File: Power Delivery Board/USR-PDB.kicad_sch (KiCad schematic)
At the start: 32 parts, among them U1 XT90, U10 Anderson PP45 Vert. 2x1, U11 Anderson PP45 Vert. 2x1, U12 TL2575HV-05IKV, U13 MCP3002-I/P, U2 LM2676T-12_NOPB, U5 Anderson PP45 Vert. 2x1, U6 Anderson PP45 Vert. 2x1, U7 Anderson PP45 Vert. 2x1, U8 Anderson PP45 Vert. 2x1, U9 Anderson PP45 Vert. 2x1

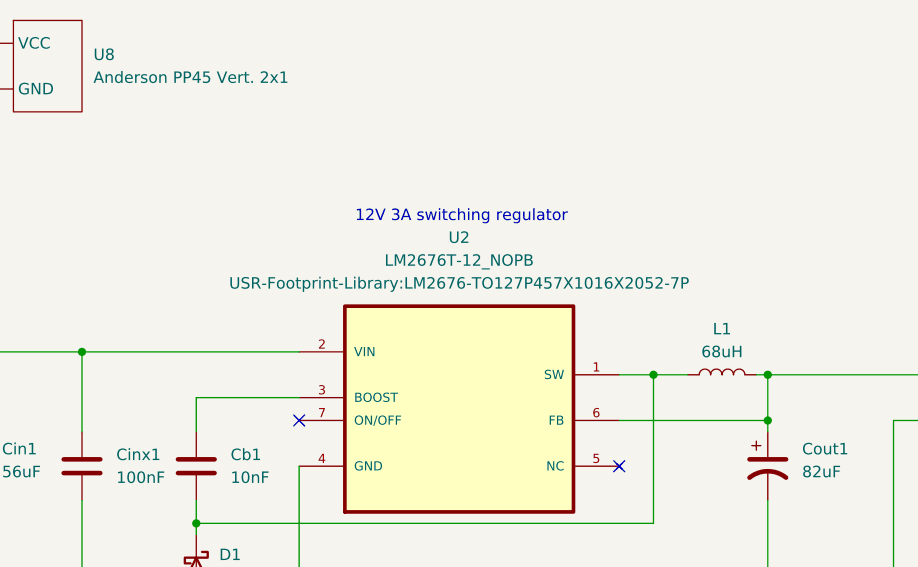
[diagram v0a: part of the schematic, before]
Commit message: Added datasheets and associated footprints to symbols
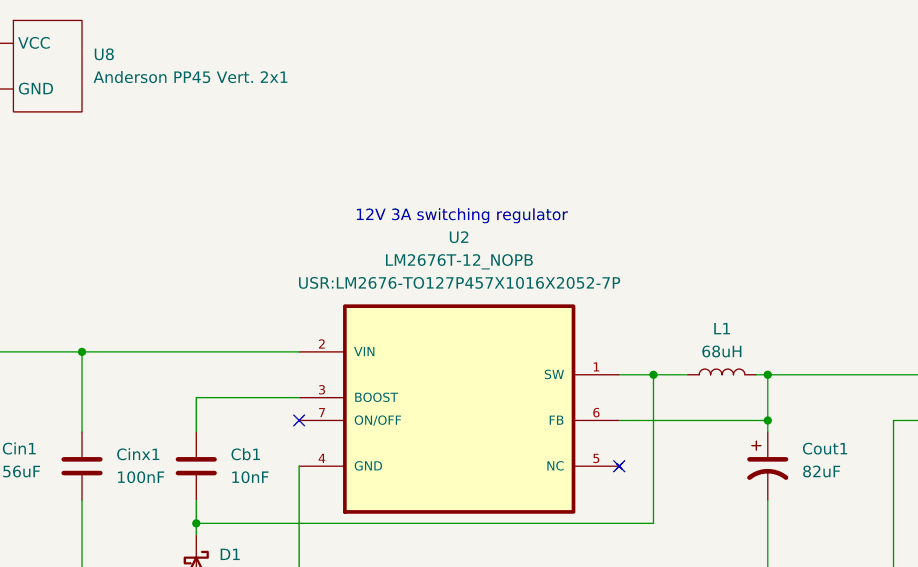
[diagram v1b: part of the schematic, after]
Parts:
- F1, F2, F3, F4, F5, F6, F7: footprint USR-Footprint-Library:FUSE_3557-15 -> USR:FUSE_3557-15
- U10, U11, U5, U6, U7, U8, U9: footprint USR-Footprint-Library:ANDERSON PP45 VERT. 2X1 -> USR:ANDERSON PP45 VERT. 2X1
- U12: footprint USR-Footprint-Library:TL2575HV-05IKV -> USR:TL2575HV-05IKV
- U13: footprint USR-Footprint-Library:PDIP8_300MC_MCH -> USR:PDIP8_300MC_MCH
- U2: footprint USR-Footprint-Library:LM2676-TO127P457X1016X2052-7P -> USR:LM2676-TO127P457X1016X2052-7P
- U3, U4: footprint USR-Footprint-Library:LKSR 50-NP -> USR:LKSR 50-NP
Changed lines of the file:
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@@
 			)
 		)
-		(property "Footprint" "USR-Footprint-Library:ANDERSON PP45 VERT. 2X1"
+		(property "Footprint" "USR:ANDERSON PP45 VERT. 2X1"
 			(at 187.96 81.28 0)
 			(effects
@@
 			)
 		)
-		(property "Footprint" "USR-Footprint-Library:FUSE_3557-15"
+		(property "Footprint" "USR:FUSE_3557-15"
 			(at 49.53 138.43 0)
 			(effects
@@
 			)
 		)
-		(property "Footprint" "USR-Footprint-Library:LKSR 50-NP"
+		(property "Footprint" "USR:LKSR 50-NP"
 			(at 157.48 87.63 0)
 			(effects
@@
 			)
 		)
-		(property "Footprint" "USR-Footprint-Library:LM2676-TO127P457X1016X2052-7P"
+		(property "Footprint" "USR:LM2676-TO127P457X1016X2052-7P"
 			(at 118.11 184.15 0)
 			(effects
@@
 			)
 		)
-		(property "Footprint" "USR-Footprint-Library:LKSR 50-NP"
+		(property "Footprint" "USR:LKSR 50-NP"
 			(at 157.48 43.18 0)
 			(effects
@@
 			)
 		)
-		(property "Footprint" "USR-Footprint-Library:FUSE_3557-15"
+		(property "Footprint" "USR:FUSE_3557-15"
 			(at 49.53 120.65 0)
 			(effects
@@
 			)
 		)
-		(property "Footprint" "USR-Footprint-Library:FUSE_3557-15"
+		(property "Footprint" "USR:FUSE_3557-15"
 			(at 49.53 157.48 0)
 			(effects
@@
 			)
 		)
-		(property "Footprint" "USR-Footprint-Library:ANDERSON PP45 VERT. 2X1"
+		(property "Footprint" "USR:ANDERSON PP45 VERT. 2X1"
 			(at 179.07 196.85 0)
 			(effects
@@
 			)
 		)
-		(property "Footprint" "USR-Footprint-Library:ANDERSON PP45 VERT. 2X1"
+		(property "Footprint" "USR:ANDERSON PP45 VERT. 2X1"
 			(at 187.96 36.83 0)
 			(effects
@@
 			)
 		)
-		(property "Footprint" "USR-Footprint-Library:ANDERSON PP45 VERT. 2X1"
+		(property "Footprint" "USR:ANDERSON PP45 VERT. 2X1"
 			(at 71.12 160.02 0)
 			(effects
@@
 			)
 		)
-		(property "Footprint" "USR-Footprint-Library:ANDERSON PP45 VERT. 2X1"
+		(property "Footprint" "USR:ANDERSON PP45 VERT. 2X1"
 			(at 71.12 140.97 0)
 			(effects
@@
 			)
 		)
-		(property "Footprint" "USR-Footprint-Library:TL2575HV-05IKV"
+		(property "Footprint" "USR:TL2575HV-05IKV"
 			(at 279.4 195.58 0)
 			(effects
@@
 			)
 		)
-		(property "Footprint" "USR-Footprint-Library:ANDERSON PP45 VERT. 2X1"
+		(property "Footprint" "USR:ANDERSON PP45 VERT. 2X1"
 			(at 71.12 104.14 0)
 			(effects
@@
 			)
 		)
-		(property "Datasheet" ""
+		(property "Datasheet" "https://www.andersonpower.com/content/dam/app/ecommerce/product-pdfs/pp/ds-pp1545.pdf"
 			(at 71.12 104.14 0)
 			(effects
@@
 			)
 		)
-		(property "Description" ""
+		(property "Description" "Anderson connectors"
 			(at 71.12 104.14 0)
 			(effects
@@
 			)
 		)
-		(property "Footprint" "USR-Footprint-Library:FUSE_3557-15"
+		(property "Footprint" "USR:FUSE_3557-15"
 			(at 49.53 101.6 0)
 			(effects
@@
 			)
 		)
-		(property "Footprint" "USR-Footprint-Library:FUSE_3557-15"
+		(property "Footprint" "USR:FUSE_3557-15"
 			(at 49.53 176.53 0)
 			(effects
@@
 			)
 		)
-		(property "Footprint" "USR-Footprint-Library:FUSE_3557-15"
+		(property "Footprint" "USR:FUSE_3557-15"
 			(at 49.53 82.55 0)
 			(effects
@@
 			)
 		)
-		(property "Footprint" "USR-Footprint-Library:ANDERSON PP45 VERT. 2X1"
+		(property "Footprint" "USR:ANDERSON PP45 VERT. 2X1"
 			(at 71.12 123.19 0)
 			(effects
@@
 			)
 		)
-		(property "Footprint" "USR-Footprint-Library:PDIP8_300MC_MCH"
+		(property "Footprint" "USR:PDIP8_300MC_MCH"
 			(at 294.64 48.26 0)
 			(effects
@@
 			)
 		)
-		(property "Footprint" "USR-Footprint-Library:FUSE_3557-15"
+		(property "Footprint" "USR:FUSE_3557-15"
 			(at 49.53 63.5 0)
 			(effects

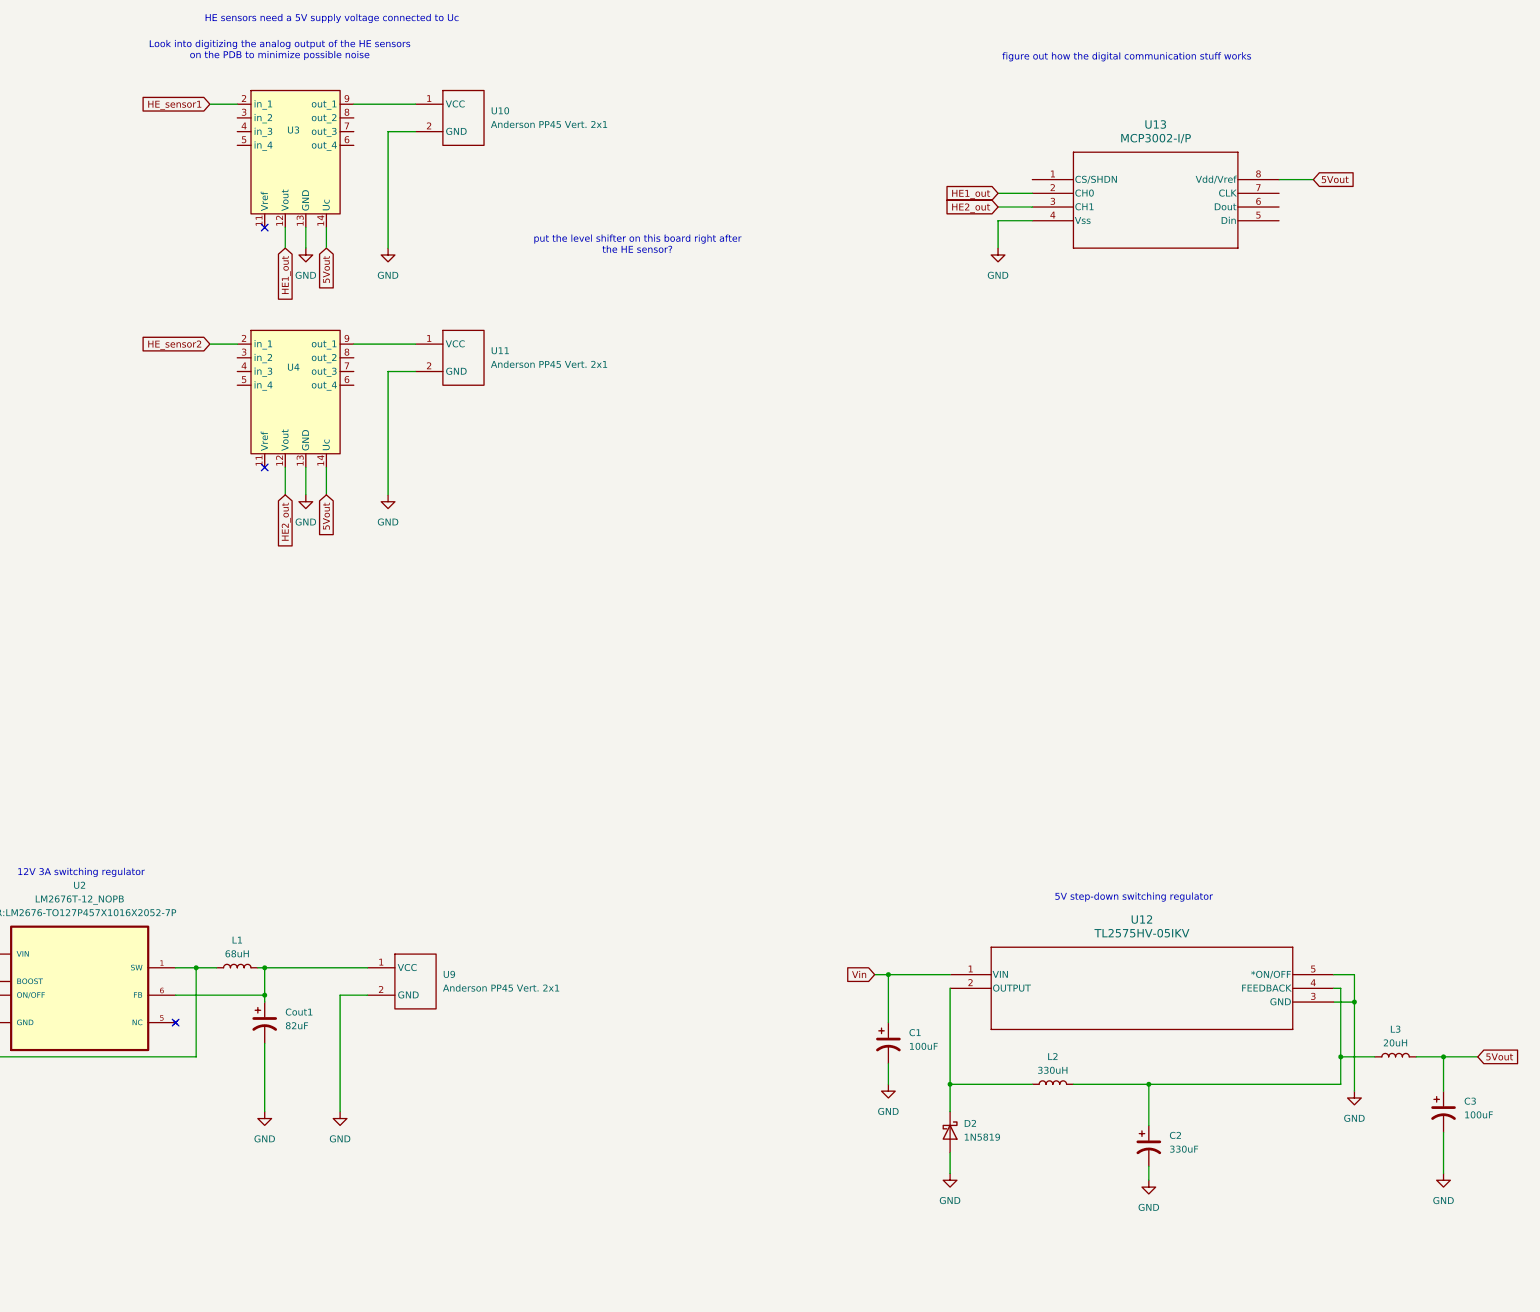
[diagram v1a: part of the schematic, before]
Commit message: PDB: added footprint for D2
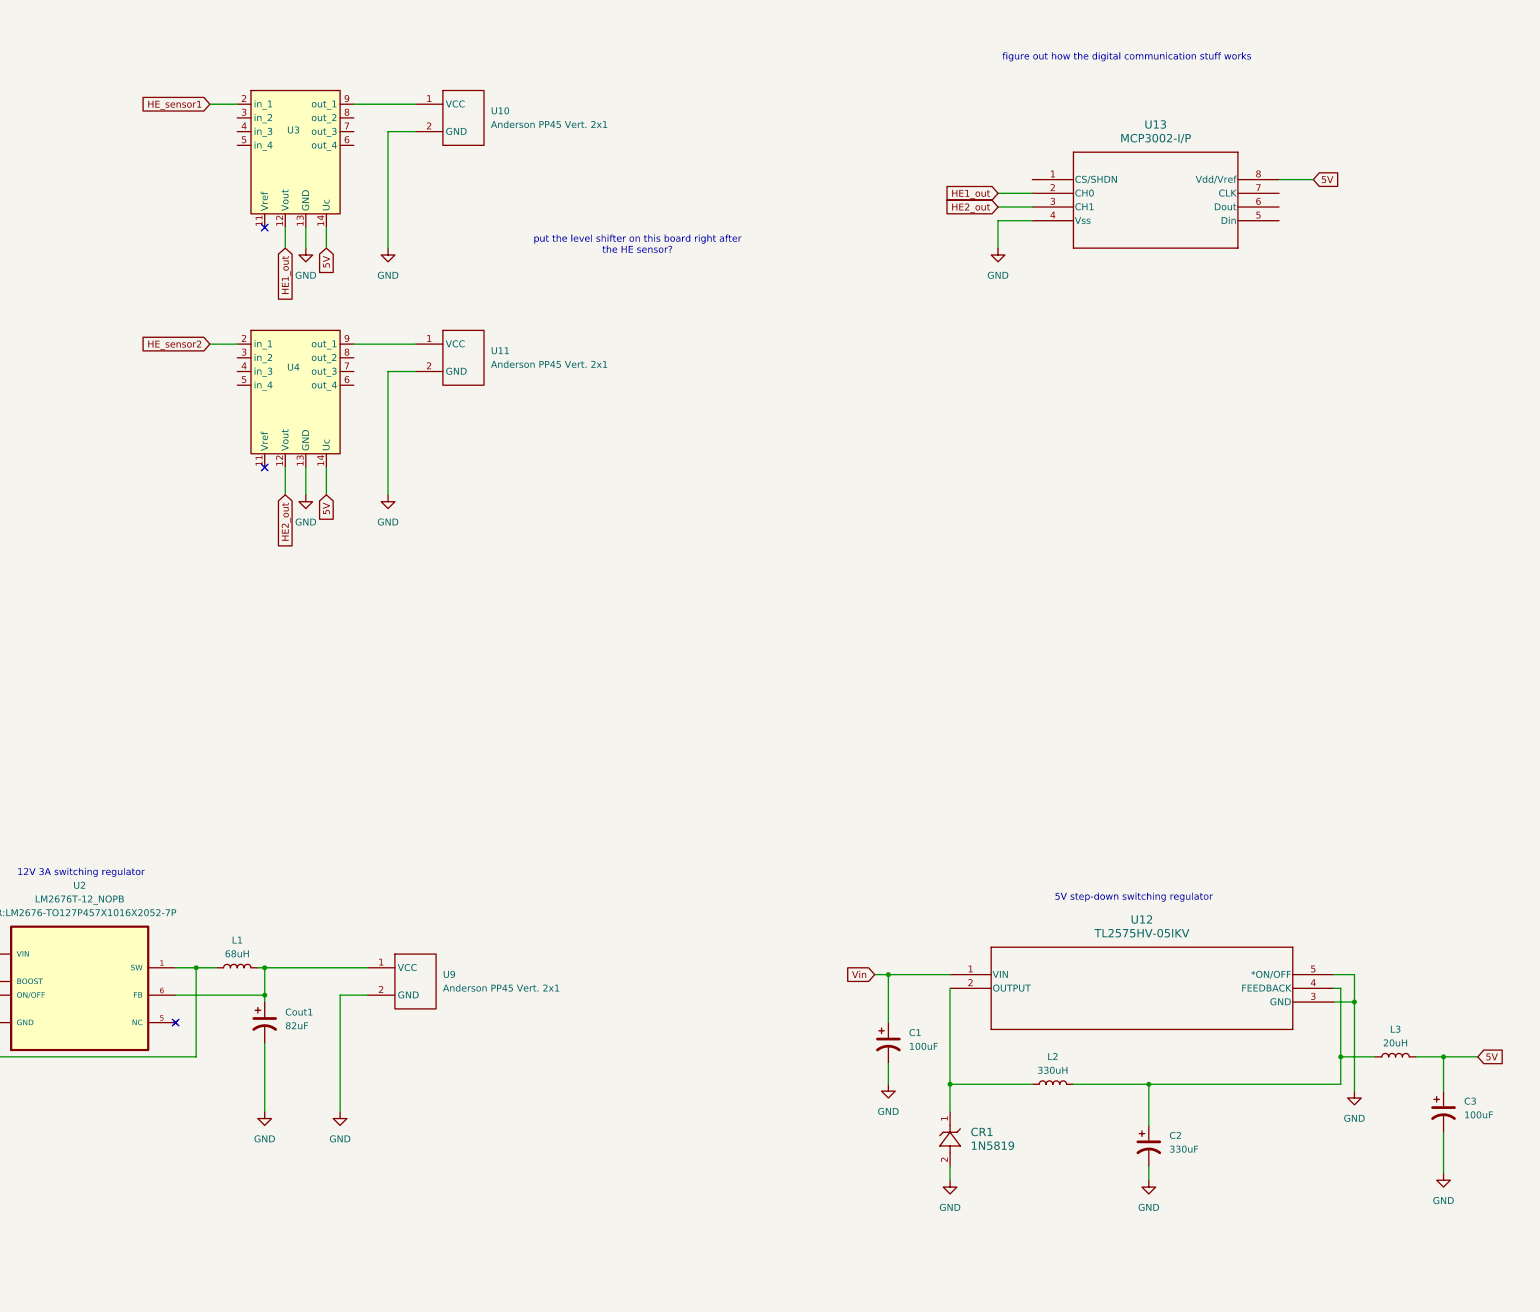
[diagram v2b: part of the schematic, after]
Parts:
- removed D2: 1N5819, symbol Device:D_Schottky
- added CR1: 1N5819, USR:DO-41_STM, symbol USR:1N5819
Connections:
- net GND: now also CR1.2
- net at L2.1, U12.2 (OUTPUT): now also CR1.1
- net 5Vout renamed 5V
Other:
- note removed: "HE sensors need a 5V supply voltage connected to Uc"
- note removed: "Look into digitizing the analog output of the HE sensors on the PDB to minimize possible noise"
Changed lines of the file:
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@@
 		)
 	)
-	(text "HE sensors need a 5V supply voltage connected to Uc\n"
-		(exclude_from_sim no)
-		(at 164.846 18.542 0)
-		(effects
-			(font
-				(size 1.27 1.27)
-			)
-		)
-	)
 	(text "2/5/2026\n"
 		(exclude_from_sim no)
@@
 		)
 	)
-	(text "Look into digitizing the analog output of the HE sensors\non the PDB to minimize possible noise\n"
-		(exclude_from_sim no)
-		(at 155.194 24.384 0)
-		(effects
-			(font
-				(size 1.27 1.27)
-			)
-		)
-	)
 	(text "put the level shifter on this board right after\nthe HE sensor?\n"
 		(exclude_from_sim no)
@@
 	(wire
 		(pts
+			(xy 279.4 231.14) (xy 279.4 233.68)
+		)
+		(stroke
+			(width 0)
+			(type default)
+		)
+	)
+	(wire
+		(pts
 			(xy 160.02 101.6) (xy 160.02 106.68)
 		)
@@
 	(wire
 		(pts
-			(xy 279.4 228.6) (xy 279.4 232.41)
-		)
-		(stroke
-			(width 0)
-			(type default)
-		)
-	)
-	(wire
-		(pts
 			(xy 288.29 53.34) (xy 294.64 53.34)
 		)
@@
 		)
 	)
-	(global_label "5Vout"
+	(global_label "5V"
 		(shape input)
 		(at 346.71 48.26 0)
@@
 		)
 		(property "Intersheetrefs" "${INTERSHEET_REFS}"
-			(at 355.017 48.26 0)
+			(at 351.9933 48.26 0)
 			(effects
 				(font
@@
 		)
 	)
-	(global_label "5Vout"
+	(global_label "5V"
 		(shape input)
 		(at 163.83 106.68 270)
@@
 		)
 		(property "Intersheetrefs" "${INTERSHEET_REFS}"
-			(at 163.83 114.987 90)
+			(at 163.83 111.9633 90)
 			(effects
 				(font
@@
 		)
 	)
-	(global_label "5Vout"
+	(global_label "5V"
 		(shape input)
 		(at 163.83 60.96 270)
@@
 		)
 		(property "Intersheetrefs" "${INTERSHEET_REFS}"
-			(at 163.83 69.267 90)
+			(at 163.83 66.2433 90)
 			(effects
 				(font
@@
 		)
 	)
-	(global_label "5Vout"
+	(global_label "5V"
 		(shape input)
 		(at 377.19 210.82 0)
@@
 		)
 		(property "Intersheetrefs" "${INTERSHEET_REFS}"
-			(at 385.497 210.82 0)
+			(at 382.4733 210.82 0)
 			(effects
 				(font
@@
 	)
 	(symbol
+		(lib_id "USR:1N5819")
+		(at 279.4 220.98 270)
+		(unit 1)
+		(exclude_from_sim no)
+		(in_bom yes)
+		(on_board yes)
+		(dnp no)
+		(fields_autoplaced yes)
+		(property "Reference" "CR1"
+			(at 283.21 224.7899 90)
+			(effects
+				(font
+					(size 1.524 1.524)
+				)
+				(justify left)
+			)
+		)
+		(property "Value" "1N5819"
+			(at 283.21 227.3299 90)
+			(effects
+				(font
+					(size 1.524 1.524)
+				)
+				(justify left)
+			)
+		)
+		(property "Footprint" "USR:DO-41_STM"
+			(at 279.4 220.98 0)
+			(effects
+				(font
+					(size 1.27 1.27)
+					(italic yes)
+				)
+				(hide yes)
+			)
+		)
+		(property "Datasheet" "https://www.st.com/resource/en/datasheet/1n5817.pdf"
+			(at 279.4 220.98 0)
+			(effects
+				(font
+					(size 1.27 1.27)
+					(italic yes)
+				)
+				(hide yes)
+			)
+		)
+		(property "Description" "40V 1A Schottky diode"
+			(at 279.4 220.98 0)
+			(effects
+				(font
+					(size 1.27 1.27)
+				)
+				(hide yes)
+			)
+		)
+		(pin "2"
+		)
+		(pin "1"
+		)
+		(instances
+			(project ""
+				(path "/f68b009f-fb0c-4740-82e4-ffb6e04b94c2"
+					(reference "CR1")
+					(unit 1)
+				)
+			)
+		)
+	)
+	(symbol
 		(lib_id "power:GND")
 		(at 288.29 60.96 0)
@@
 	)
 	(symbol
-		(lib_id "power:GND")
-		(at 279.4 232.41 0)
-		(unit 1)
-		(exclude_from_sim no)
-		(in_bom yes)
-		(on_board yes)
-		(dnp no)
-		(fields_autoplaced yes)
-		(property "Reference" "#PWR014"
-			(at 279.4 238.76 0)
-			(effects
-				(font
-					(size 1.27 1.27)
-				)
-				(hide yes)
-			)
-		)
-		(property "Value" "GND"
-			(at 279.4 237.49 0)
-			(effects
-				(font
-					(size 1.27 1.27)
-				)
-			)
-		)
-		(property "Footprint" ""
-			(at 279.4 232.41 0)
-			(effects
-				(font
-					(size 1.27 1.27)
-				)
-				(hide yes)
-			)
-		)
-		(property "Datasheet" ""
-			(at 279.4 232.41 0)
-			(effects
-				(font
-					(size 1.27 1.27)
-				)
-				(hide yes)
-			)
-		)
-		(property "Description" "Power symbol creates a global label with name \"GND\" , ground"
-			(at 279.4 232.41 0)
-			(effects
-				(font
-					(size 1.27 1.27)
-				)
-				(hide yes)
-			)
-		)
-		(pin "1"
-		)
-		(instances
-			(project ""
-				(path "/f68b009f-fb0c-4740-82e4-ffb6e04b94c2"
-					(reference "#PWR014")
-					(unit 1)
-				)
-			)
-		)
-	)
-	(symbol
 		(lib_id "USR_SymLibrary:root_0_Anderson_PP45_Vert._2x1_")
 		(at 179.07 196.85 0)
@@
 	)
 	(symbol
+		(lib_id "power:GND")
+		(at 279.4 233.68 0)
+		(unit 1)
+		(exclude_from_sim no)
+		(in_bom yes)
+		(on_board yes)
+		(dnp no)
+		(fields_autoplaced yes)
+		(property "Reference" "#PWR014"
+			(at 279.4 240.03 0)
+			(effects
+				(font
+					(size 1.27 1.27)
+				)
+				(hide yes)
+			)
+		)
+		(property "Value" "GND"
+			(at 279.4 238.76 0)
+			(effects
+				(font
+					(size 1.27 1.27)
+				)
+			)
+		)
+		(property "Footprint" ""
+			(at 279.4 233.68 0)
+			(effects
+				(font
+					(size 1.27 1.27)
+				)
+				(hide yes)
+			)
+		)
+		(property "Datasheet" ""
+			(at 279.4 233.68 0)
+			(effects
+				(font
+					(size 1.27 1.27)
+				)
+				(hide yes)
+			)
+		)
+		(property "Description" "Power symbol creates a global label with name \"GND\" , ground"
+			(at 279.4 233.68 0)
+			(effects
+				(font
+					(size 1.27 1.27)
+				)
+				(hide yes)
+			)
+		)
+		(pin "1"
+		)
+		(instances
+			(project ""
+				(path "/f68b009f-fb0c-4740-82e4-ffb6e04b94c2"
+					(reference "#PWR014")
+					(unit 1)
+				)
+			)
+		)
+	)
+	(symbol
 		(lib_id "USR_SymLibrary:root_0_Anderson_PP45_Vert._2x1_")
 		(at 71.12 140.97 0)
@@
 					(unit 1)
 				)
-			)
-		)
-	)
-	(symbol
-		(lib_id "Device:D_Schottky")
-		(at 279.4 224.79 270)
-		(unit 1)
-		(exclude_from_sim no)
-		(in_bom yes)
-		(on_board yes)
-		(dnp no)
-		(fields_autoplaced yes)
-		(property "Reference" "D2"
-			(at 281.94 223.2024 90)
-			(effects
-				(font
-					(size 1.27 1.27)
-				)
-				(justify left)
-			)
-		)
-		(property "Value" "1N5819"
-			(at 281.94 225.7424 90)
-			(effects
-				(font
-					(size 1.27 1.27)
-				)
-				(justify left)
-			)
-		)
-		(property "Footprint" ""
-			(at 279.4 224.79 0)
-			(effects
-				(font
-					(size 1.27 1.27)
-				)
-				(hide yes)
-			)
-		)
-		(property "Datasheet" "~"
-			(at 279.4 224.79 0)
-			(effects
-				(font
-					(size 1.27 1.27)
-				)
-				(hide yes)
-			)
-		)
-		(property "Description" "Schottky diode"
-			(at 279.4 224.79 0)
-			(effects
-				(font
-					(size 1.27 1.27)
-				)
-				(hide yes)
-			)
-		)
-		(pin "2"
-		)
-		(pin "1"
-		)
-		(instances
-			(project ""
-				(path "/f68b009f-fb0c-4740-82e4-ffb6e04b94c2"
-					(reference "D2")
-					(unit 1)
-				)
